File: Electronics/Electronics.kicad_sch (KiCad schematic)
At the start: 8 parts, among them J1 Barrel_Jack, M1 Motor_DC, M2 Motor_DC, M3 Motor_DC, M4 Motor_DC

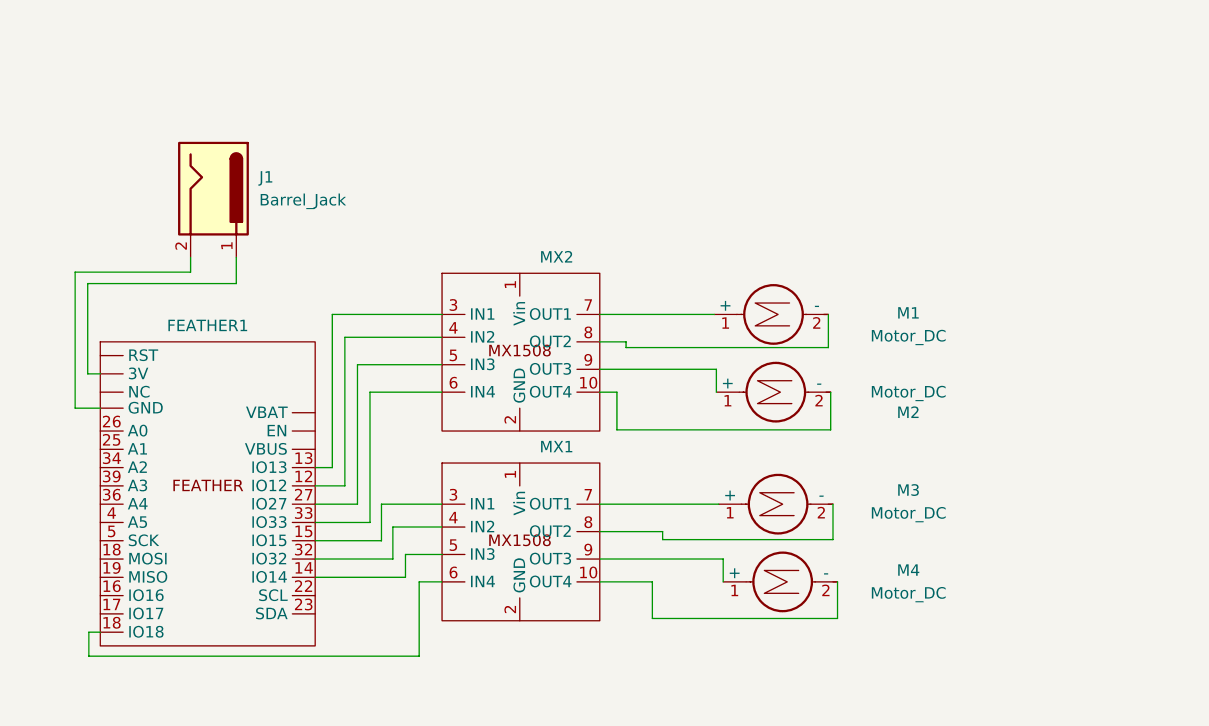
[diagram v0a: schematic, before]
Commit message: UI engineering time, added motor get function
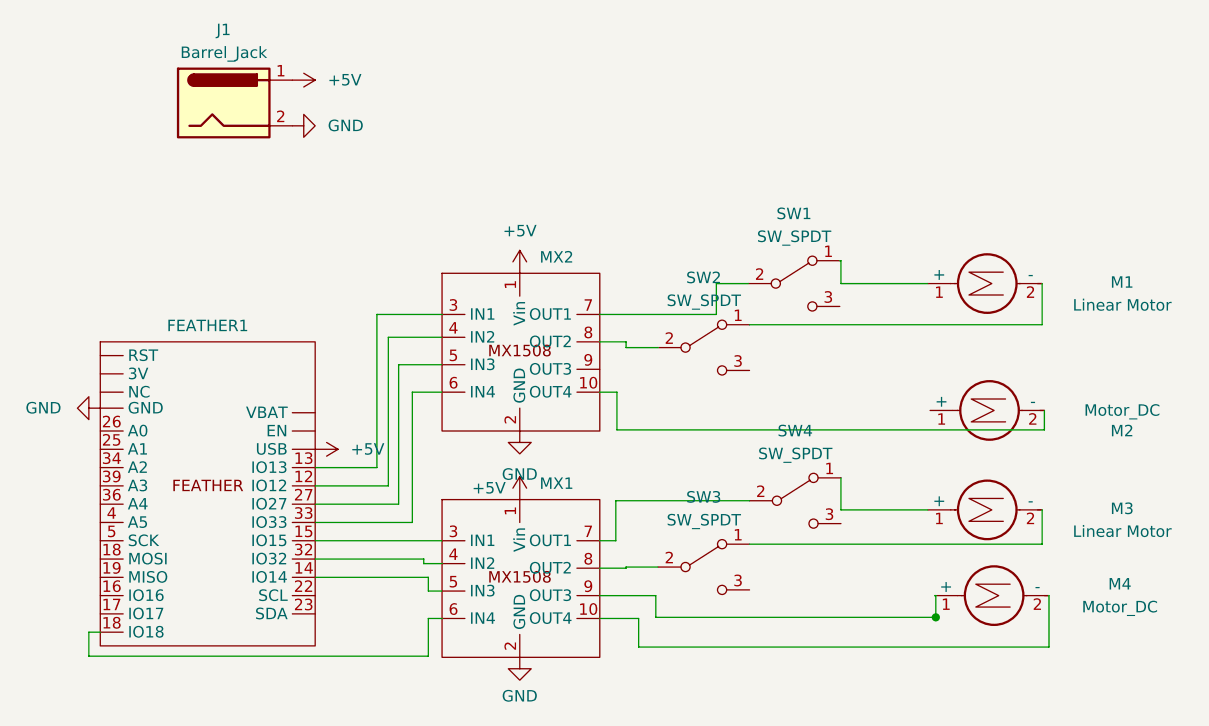
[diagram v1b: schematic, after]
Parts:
- added SW1, SW2, SW3, SW4: SW_SPDT, symbol Switch:SW_SPDT
- M1, M3: value Motor_DC -> Linear Motor
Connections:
- net at M3.1 (+): now also SW4.1 (A); no longer MX1.7 (OUT1)
- net at MX1.8 (OUT2): now also SW3.2 (B); no longer M3.2 (-)
- net at M2.1 (+): no longer MX2.9 (OUT3)
- net at M1.1 (+): now also SW1.1 (A); no longer MX2.7 (OUT1)
- net at M1.2 (-): now also SW2.1 (A); no longer MX2.8 (OUT2)
- net +5V: now reaches MX1.1 (Vin)
- net +5V: now also FEATHER1. (VBAT), J1.1, MX2.1 (Vin)
- net GND: now reaches MX1.2 (GND)
- net GND: now also FEATHER1. (VBAT), J1.2, MX2.2 (GND)
- new net: MX1.7 (OUT1), SW4.2 (B)
- new net: MX2.7 (OUT1), SW1.2 (B)
- new net: M3.2 (-), SW3.1 (A)
- new net: MX2.8 (OUT2), SW2.2 (B)
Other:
- moved on the sheet: J1, M1, M2, M4, MX1

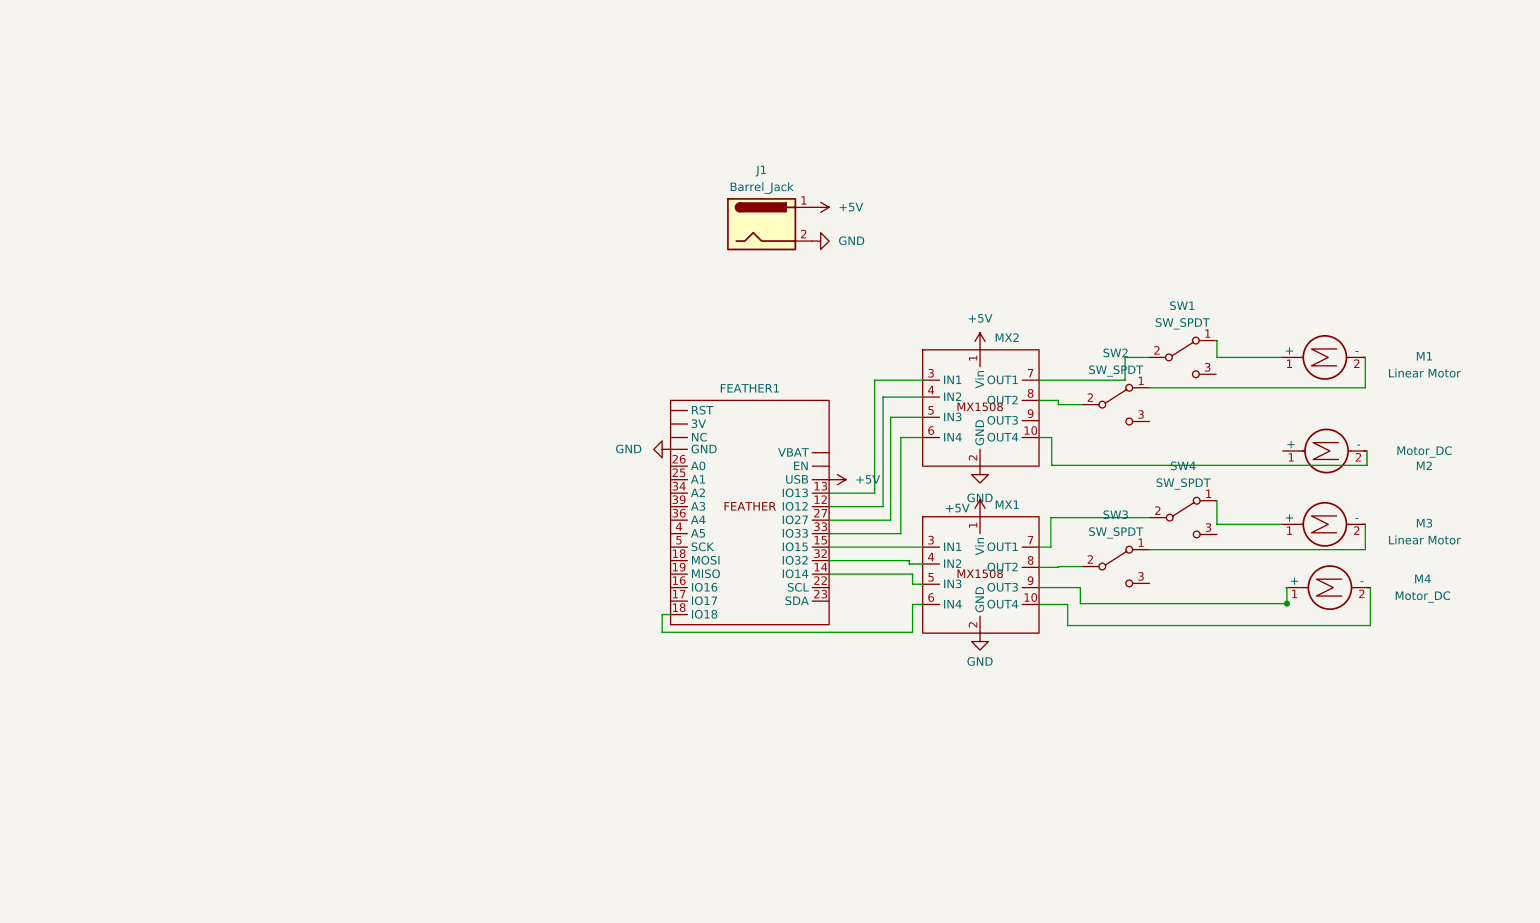
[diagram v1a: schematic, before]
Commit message: changed to phone hotspot
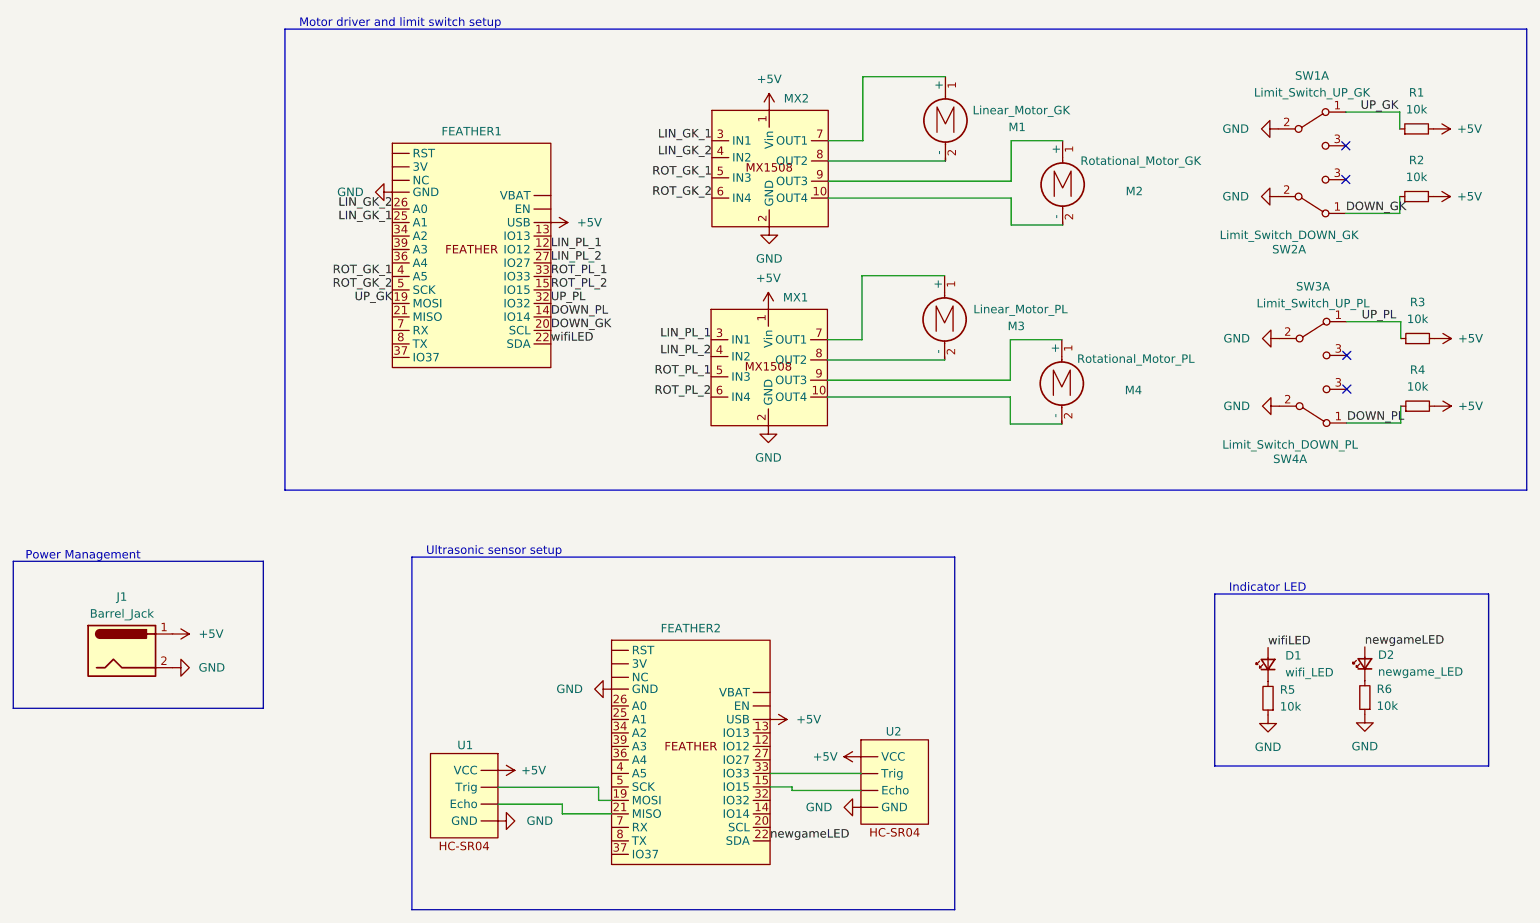
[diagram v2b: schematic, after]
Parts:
- removed SW1, SW2, SW3, SW4: SW_SPDT, symbol Switch:SW_SPDT
- added D1: wifi_LED, symbol Device:LED_Small
- added D2: newgame_LED, symbol Device:LED_Small
- added FEATHER2: ~, symbol Symbols:Adafruit_Feather
- added R1, R2, R3, R4, R5, R6: 10k, symbol Device:R_Small
- added SW1: Limit_Switch_UP_GK, symbol Switch:SW_DPDT_x2
- added SW2: Limit_Switch_DOWN_GK, symbol Switch:SW_DPDT_x2
- added SW3: Limit_Switch_UP_PL, symbol Switch:SW_DPDT_x2
- added SW4: Limit_Switch_DOWN_PL, symbol Switch:SW_DPDT_x2
- added U1, U2: ~, symbol Symbols:ultrasonic_sensor
- M1: value Linear Motor -> Linear_Motor_GK
- M2: value Motor_DC -> Rotational_Motor_GK
- M3: value Linear Motor -> Linear_Motor_PL
- M4: value Motor_DC -> Rotational_Motor_PL
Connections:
- net +5V: now also FEATHER2. (VBAT), R1.2, R2.2, R3.2, R4.2, U1. (VCC), U2. (VCC)
- net GND: now also FEATHER2. (VBAT), R5.1, R6.1, SW1.2 (B), SW2.2 (B), SW3.2 (B), SW4.2 (B), U1. (VCC), U2. (VCC)
- net at M2.1 (+): now also MX2.9 (OUT3)
- net at M3.1 (+): now also MX1.7 (OUT1)
- net at M1.1 (+): now also MX2.7 (OUT1)
- net at M1.2 (-): now also MX2.8 (OUT2)
- net LIN_PL_1: now reaches MX1.3 (IN1)
- net LIN_PL_1: now also FEATHER1.12 (IO12); no longer FEATHER1.15 (IO15)
- net LIN_PL_2: now reaches MX1.4 (IN2)
- net LIN_PL_2: now also FEATHER1.27 (IO27); no longer FEATHER1.32 (IO32)
- net DOWN_PL: now reaches FEATHER1.14 (IO14)
- net DOWN_PL: now also R4.1, SW4.1 (A); no longer MX1.5 (IN3)
- net ROT_PL_2: now reaches MX1.6 (IN4)
- net ROT_PL_2: now also FEATHER1.15 (IO15); no longer FEATHER1.18 (MOSI)
- net at MX1.8 (OUT2): now also M3.2 (-)
- net LIN_GK_2: now reaches MX2.4 (IN2)
- net LIN_GK_2: now also FEATHER1.26 (A0); no longer FEATHER1.12 (IO12)
- net at FEATHER1.13 (IO13): no longer MX2.3 (IN1)
- net UP_GK: now reaches FEATHER1.19 (MOSI)
- net UP_GK: now also R1.1, SW1.1 (A)
- net wifiLED: now reaches FEATHER1.22 (SDA)
- net wifiLED: now also D1.2 (A)
- net LIN_GK_1: now reaches FEATHER1.25 (A1)
- net LIN_GK_1: now also MX2.3 (IN1)
- net ROT_GK_1: now reaches MX2.5 (IN3)
- net ROT_GK_1: now also FEATHER1.4 (A5); no longer FEATHER1.27 (IO27)
- net ROT_GK_2: now reaches MX2.6 (IN4)
- net ROT_GK_2: now also FEATHER1.5 (SCK); no longer FEATHER1.33 (IO33)
- new net: FEATHER2.15 (IO15), U2. (VCC)
- new net: FEATHER2.19 (MOSI), U1. (VCC)
- new net: FEATHER2.21 (MISO), U1. (VCC)
- new net: FEATHER2.33 (IO33), U2. (VCC)
- new net: D1.1 (K), R5.2
- new net: D2.1 (K), R6.2
- new net DOWN_GK: FEATHER1.20 (SCL), R2.1, SW2.1 (A)
- new net ROT_PL_1: FEATHER1.33 (IO33), MX1.5 (IN3)
- new net UP_PL: FEATHER1.32 (IO32), R3.1, SW3.1 (A)
- new net newgameLED: D2.2 (A), FEATHER2.22 (SDA)
- no-connect marks 0 -> 4
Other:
- note added: "Indicator LED"
- note added: "Motor driver and limit switch setup"
- note added: "Power Management"
- note added: "Ultrasonic sensor setup"
- moved on the sheet: J1, M1
